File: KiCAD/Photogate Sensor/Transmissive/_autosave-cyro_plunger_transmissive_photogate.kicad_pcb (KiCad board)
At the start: 2 copper layers, 122 x 70 mm, 46 parts, among them J2 FFC Socket, J3 USB_B_Micro, J4 UPDI socket, J6 Conn_01x03_Socket, Q1 Q_NMOS_GSD, Q2 Q_NMOS_GSD, Q3 Q_NMOS_GSD, Q4 Q_NMOS_GSD, U1 5V LDO, U2 Opamp_Dual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

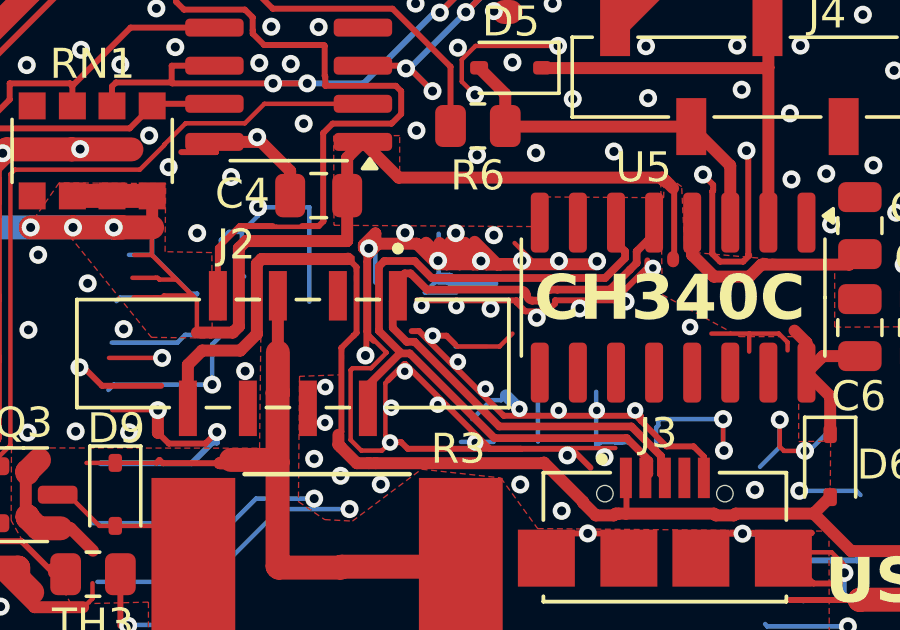
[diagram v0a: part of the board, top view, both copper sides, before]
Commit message: Add skew on power board D+ to offset skew on photogate board
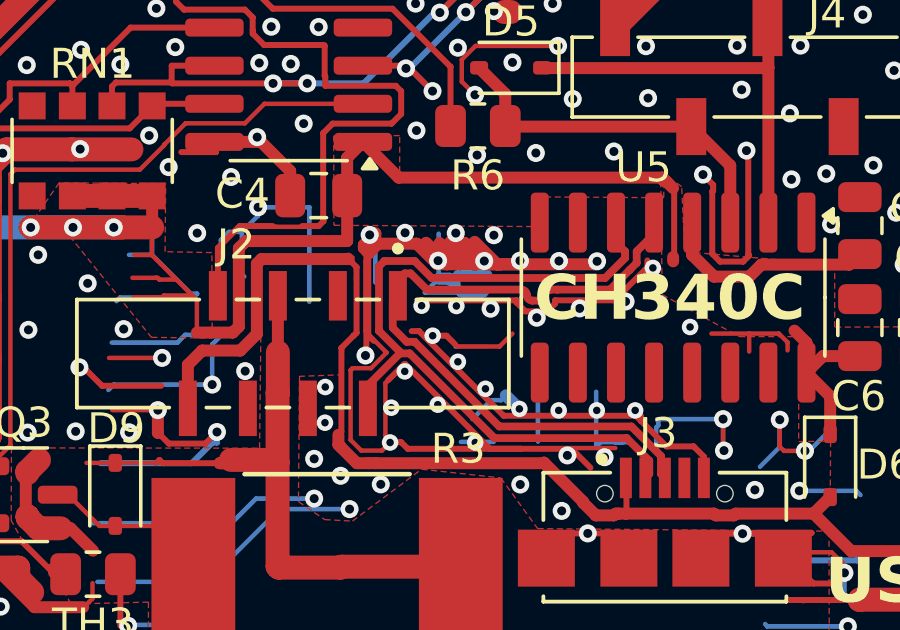
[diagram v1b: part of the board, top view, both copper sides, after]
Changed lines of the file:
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@@
 	)
 	(segment
-		(start 179.73 156.38)
-		(end 180.51 157.16)
-		(width 0.15)
-		(layer "F.Cu")
-		(net 2)
-	)
-	(segment
 		(start 193.2 147.65)
 		(end 197.4 147.65)
@@
 	)
 	(via
-		(at 178.61 156.98)
+		(at 178.72 156.98)
 		(size 0.6)
 		(drill 0.3)
@@
 	)
 	(via
-		(at 174.87 156.56)
+		(at 174.9 156.11)
 		(size 0.6)
 		(drill 0.3)
@@
 	)
 	(via
-		(at 179.98 156.97)
+		(at 179.91 156.97)
 		(size 0.6)
 		(drill 0.3)
@@
 	)
 	(segment
+		(start 177.73 157.74)
+		(end 177.75 157.74)
+		(width 0.2)
+		(layer "B.Cu")
+		(net 2)
+	)
+	(segment
 		(start 134.9 124.98)
 		(end 134.9 123.63)
@@
 	)
 	(segment
-		(start 177.73 157.74)
-		(end 178.99 157.74)
-		(width 0.4)
-		(layer "B.Cu")
-		(net 2)
-	)
-	(segment
 		(start 184.52 162.46)
 		(end 184.45 162.53)
@@
 	)
 	(segment
+		(start 177.7 157.62)
+		(end 177.84 157.48)
+		(width 0.15)
+		(layer "B.Cu")
+		(net 2)
+	)
+	(segment
 		(start 130.35 124.81)
 		(end 127.48 124.81)
@@
 	)
 	(segment
+		(start 177.75 157.74)
+		(end 177.97 157.96)
+		(width 0.2)
+		(layer "B.Cu")
+		(net 2)
+	)
+	(segment
 		(start 169.97 159.44)
 		(end 168.75 159.44)
@@
 	)
 	(segment
+		(start 177.97 158.01)
+		(end 178.67 158.01)
+		(width 0.4)
+		(layer "B.Cu")
+		(net 2)
+	)
+	(segment
 		(start 169.15 158.07)
 		(end 169.02 158.2)
@@
 	)
 	(segment
+		(start 178.76 161.24)
+		(end 178.75 161.24)
+		(width 0.4)
+		(layer "B.Cu")
+		(net 2)
+	)
+	(segment
 		(start 177.2 156.99)
 		(end 177.2 157.46)
@@
 	)
 	(segment
+		(start 177.86 157.47)
+		(end 178.8 157.47)
+		(width 0.4)
+		(layer "B.Cu")
+		(net 2)
+	)
+	(segment
 		(start 202.03 120.13)
 		(end 202.03 121.72)
@@
 	)
 	(segment
+		(start 178.865 161.665)
+		(end 177.97 160.77)
+		(width 0.15)
+		(layer "B.Cu")
+		(net 2)
+	)
+	(segment
 		(start 170.25 165.72)
 		(end 165.66 165.72)
@@
 	)
 	(segment
-		(start 177.24 156.96)
-		(end 179.14 156.96)
-		(width 0.2)
-		(layer "B.Cu")
-		(net 2)
-	)
-	(segment
 		(start 171.18 155.19)
 		(end 171.18 155.47)
@@
 	)
 	(segment
+		(start 178.865 161.675)
+		(end 178.865 161.665)
+		(width 0.15)
+		(layer "B.Cu")
+		(net 2)
+	)
+	(segment
+		(start 177.61 157.62)
+		(end 177.7 157.62)
+		(width 0.15)
+		(layer "B.Cu")
+		(net 2)
+	)
+	(segment
 		(start 175.09 156.06)
 		(end 175.09 157.7)
@@
 	)
 	(segment
+		(start 177.84 157.48)
+		(end 177.89 157.53)
+		(width 0.2)
+		(layer "B.Cu")
+		(net 2)
+	)
+	(segment
 		(start 125.46 124.98)
 		(end 123.17 124.98)
@@
 	)
 	(segment
+		(start 177.89 157.53)
+		(end 177.9 157.52)
+		(width 0.2)
+		(layer "B.Cu")
+		(net 2)
+	)
+	(segment
+		(start 177.56 157.57)
+		(end 177.61 157.62)
+		(width 0.15)
+		(layer "B.Cu")
+		(net 2)
+	)
+	(segment
 		(start 132.32 124.81)
 		(end 135.28 127.77)
@@
 	)
 	(segment
+		(start 178.95 161.62)
+		(end 178.895 161.675)
+		(width 0.15)
+		(layer "B.Cu")
+		(net 2)
+	)
+	(segment
 		(start 183.08 163.02)
 		(end 182.6 163.02)
@@
 		(layer "B.Cu")
 		(net 2)
+	)
+	(segment
+		(start 178.895 161.675)
+		(end 178.865 161.675)
+		(width 0.15)
+		(layer "B.Cu")
+		(net 2)
